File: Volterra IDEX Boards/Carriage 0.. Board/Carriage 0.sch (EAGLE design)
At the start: 28 parts, among them K1 FFC/FPC/34PIN/1MMPITCH/TOPLOCK, K2 FFC/FPC/34PIN/1MMPITCH/TOPLOCK, K3 FFC/FPC/34PIN/1MMPITCH/TOPLOCK

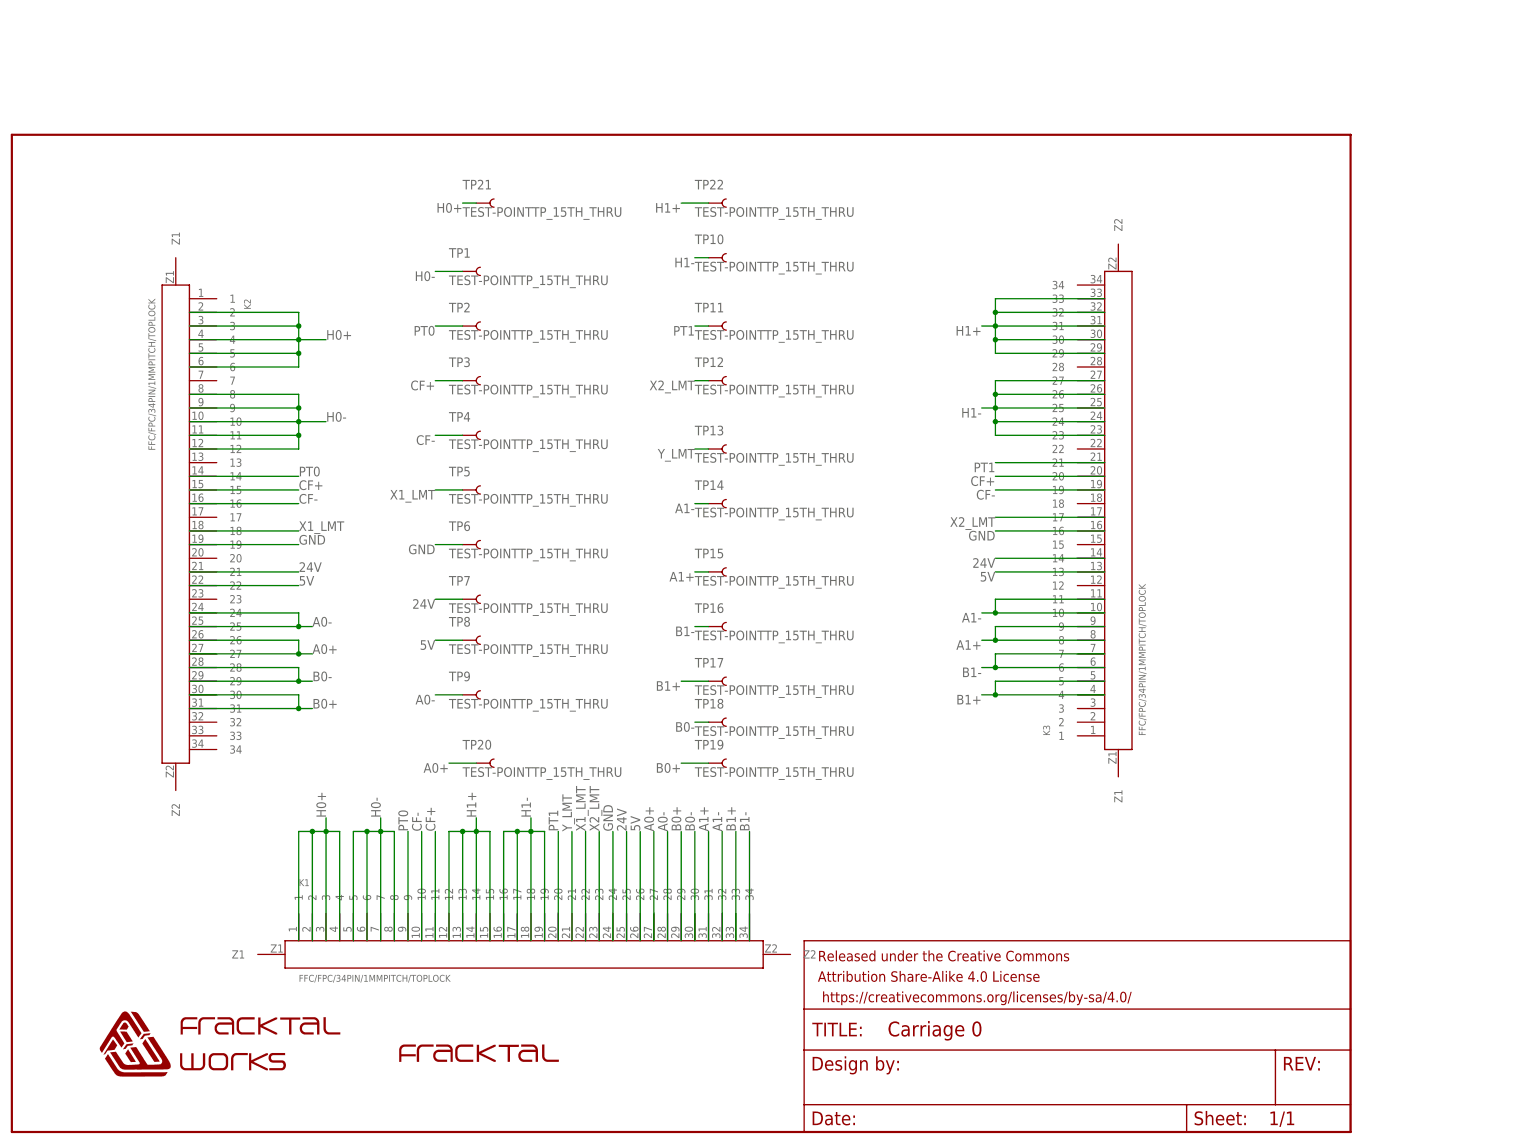
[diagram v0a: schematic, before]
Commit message: Switching of carriage board numbering, changing extruder FFC pins and fixing routings
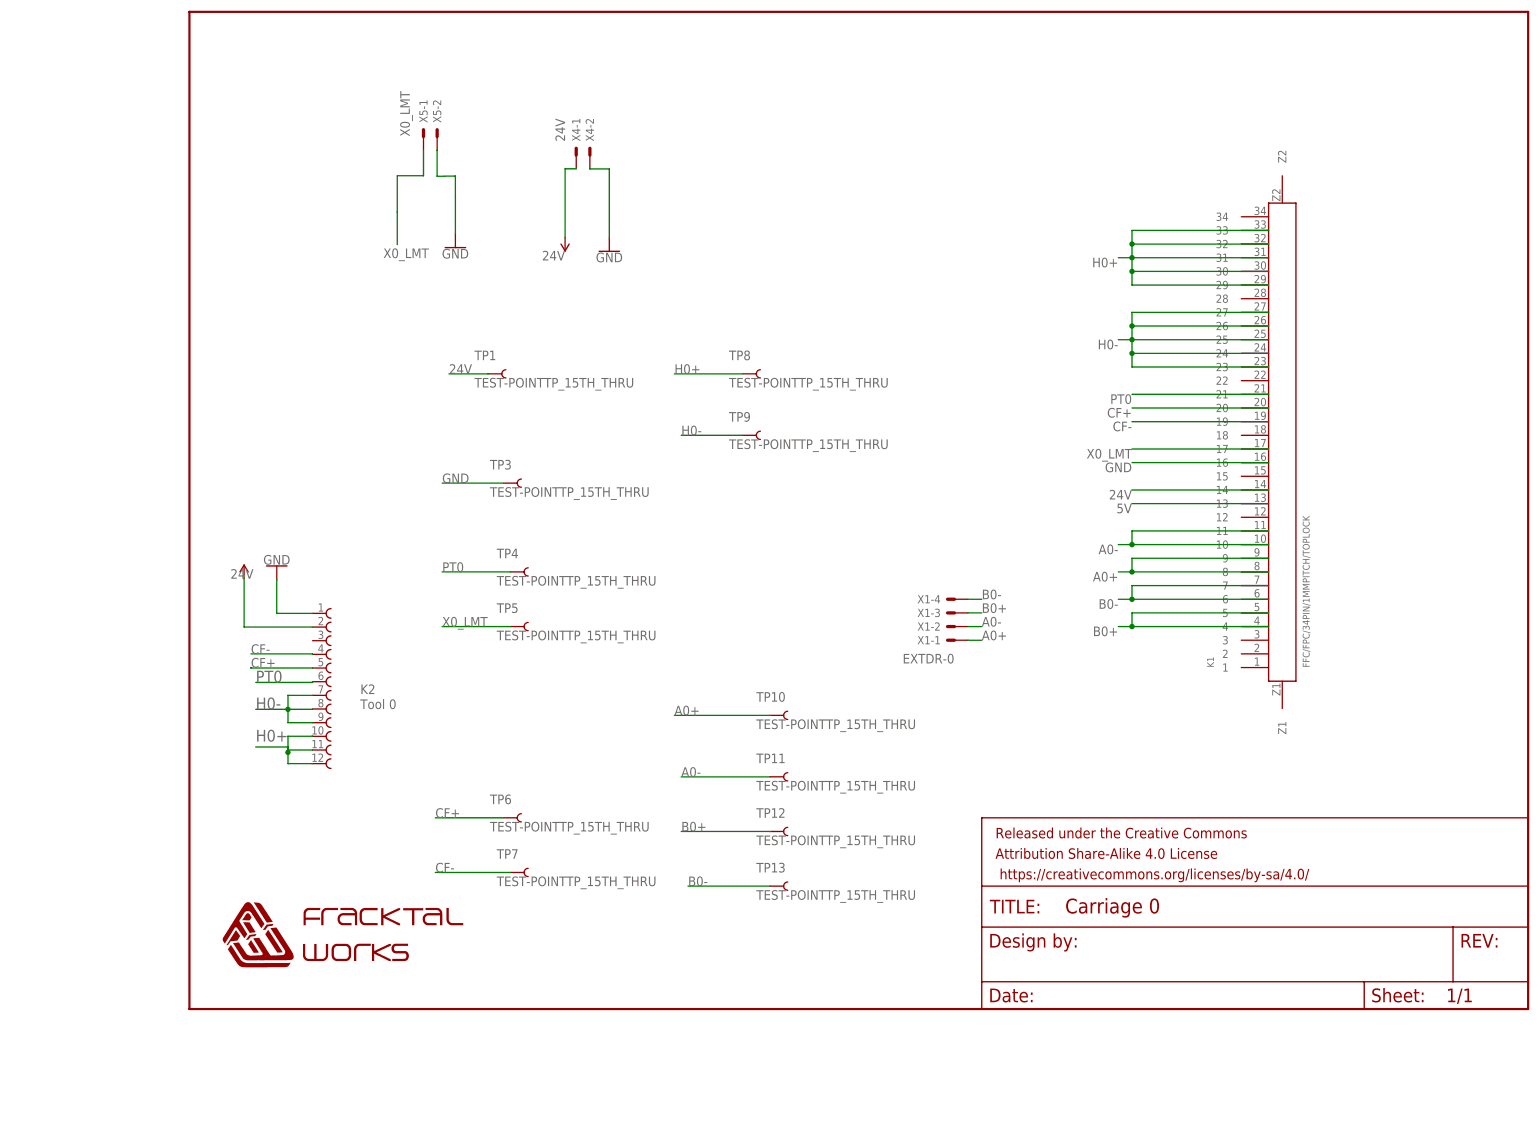
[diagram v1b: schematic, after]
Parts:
- removed K3: FFC/FPC/34PIN/1MMPITCH/TOPLOCK, FracktalWorks_Eagle_Library:FFC/FPC/34PIN/1MMPITCH/TOPLOCK
- removed TP14, TP15, TP16, TP17, TP18, TP19, TP2, TP20, TP21, TP22: TEST-POINTTP_15TH_THRU, SparkFun-Connectors:TEST-POINTTP_15TH_THRU
- removed U$1: FWLOGO, FracktalWorks_Eagle_Library:FWLOGO
- added X1: EXTDR-0, Rembrandt Electronics - JST XH Connectors v1-0:JST-XH-04-PIN-LONG-PAD
- added X4: 24V, Rembrandt Electronics - JST XH Connectors v1-0:JST-XH-02-PIN-LONG-PAD
- added X5: X_LMT, Rembrandt Electronics - JST XH Connectors v1-0:JST-XH-02-PIN-LONG-PAD
- K2: value FFC/FPC/34PIN/1MMPITCH/TOPLOCK -> Tool 0; device FracktalWorks_Eagle_Library:FFC/FPC/34PIN/1MMPITCH/TOPLOCK -> Wurth_Elektronik_Electromechanic_FPC_Connectors_&_Flat_Flexible_Cable_rev15b:68611214122
- U$2: value FRACKTALLOGO -> FWLOGO; device FracktalWorks_Eagle_Library:FRACKTALLOGO -> FracktalWorks_Eagle_Library:FWLOGO
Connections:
- removed net A1+: K1.31, K3.8, K3.9, TP15.1
- removed net A1-: K1.32, K3.10, K3.11, TP14.1
- removed net B1+: K1.33, K3.4, K3.5, TP17.1
- removed net B1-: K1.34, K3.6, K3.7, TP16.1
- removed net H1+: K1.12, K1.13, K1.14, K1.15, K3.29, K3.30, K3.31, K3.32, K3.33, TP22.1
- removed net H1-: K1.16, K1.17, K1.18, K1.19, K3.23, K3.24, K3.25, K3.26, K3.27, TP10.1
- removed net PT1: K1.20, K3.21, TP11.1
- removed net X1_LMT: K1.22, K2.18, TP5.1
- removed net X2_LMT: K1.23, K3.17, TP12.1
- removed net Y_LMT: K1.21, TP13.1
- new net X0_LMT: K1.17, TP5.1, X5-1.S
- net 24V: now also K1.14, K2.2, TP1.1, X4-1.S; no longer K1.25, K2.21, K3.14, TP7.1
- net 5V: now also K1.13; no longer K1.26, K2.22, K3.13, TP8.1
- net A0+: now also K1.8, K1.9, TP10.1, X1-1.S; no longer K1.27, K2.26, K2.27, TP20.1
- net A0-: now also K1.10, K1.11, TP11.1, X1-2.S; no longer K1.28, K2.24, K2.25, TP9.1
- net B0+: now also K1.4, K1.5, TP12.1, X1-3.S; no longer K1.29, K2.30, K2.31, TP19.1
- net B0-: now also K1.6, K1.7, TP13.1, X1-4.S; no longer K1.30, K2.28, K2.29, TP18.1
- net CF+: now also K1.20, K2.5, TP6.1; no longer K1.11, K2.15, K3.20, TP3.1
- net CF-: now also K1.19, K2.4, TP7.1; no longer K1.10, K2.16, K3.19, TP4.1
- net GND: now also K1.16, K2.1, TP3.1, X4-2.S, X5-2.S; no longer K1.24, K2.19, K3.16, TP6.1
- net H0+: now also K1.29, K1.30, K1.31, K1.32, K1.33, K2.10, K2.11, K2.12, TP8.1; no longer K1.1, K1.2, K1.3, K1.4, K2.2, K2.3, K2.4, K2.5, K2.6, TP21.1
- net H0-: now also K1.23, K1.24, K1.25, K1.26, K1.27, K2.7, TP9.1; no longer K1.5, K1.6, K1.7, K1.8, K2.10, K2.11, K2.12, TP1.1
- net PT0: now also K1.21, K2.6, TP4.1; no longer K1.9, K2.14, TP2.1
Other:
- moved on the sheet: K1, TP1, TP10, TP11, TP12, TP13, TP3, TP4, TP5, TP6, TP7, TP8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

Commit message: Updated Daughter board schematic and other boards
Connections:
- net 5V: now also K2.3
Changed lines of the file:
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@@
 <label x="215.9" y="116.84" size="1.778" layer="95" rot="R180"/>
+</segment>
+<segment>
+<pinref part="K2" gate="G$1" pin="3"/>
+<wire x1="63.52" y1="91.35" x2="53.34" y2="91.35" width="0.1524" layer="91"/>
+<wire x1="53.34" y1="91.35" x2="53.34" y2="91.44" width="0.1524" layer="91"/>
+<label x="53.34" y="91.44" size="1.778" layer="95"/>
 </segment>
 </net>
